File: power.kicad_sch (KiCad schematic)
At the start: 161 parts, among them Q10 SI7613DN-T1-GE3, Q14 BC817-25W, Q15 BC817-25W, Q2 BC817-25W, Q3 DZDH0401DW, Q4 DZDH0401DW, Q5 SI7613DN-T1-GE3, Q6 SI7613DN-T1-GE3, Q7 BC817-25W, Q8 BC817-25W, Q9 SI7613DN-T1-GE3, U1 LT8350RV#PBF, U10 LM3881MME_NOPB, U2 MP2386GG, U3 TPS65983BAZBHR, U9 LM1117MP-3.3_NOPB

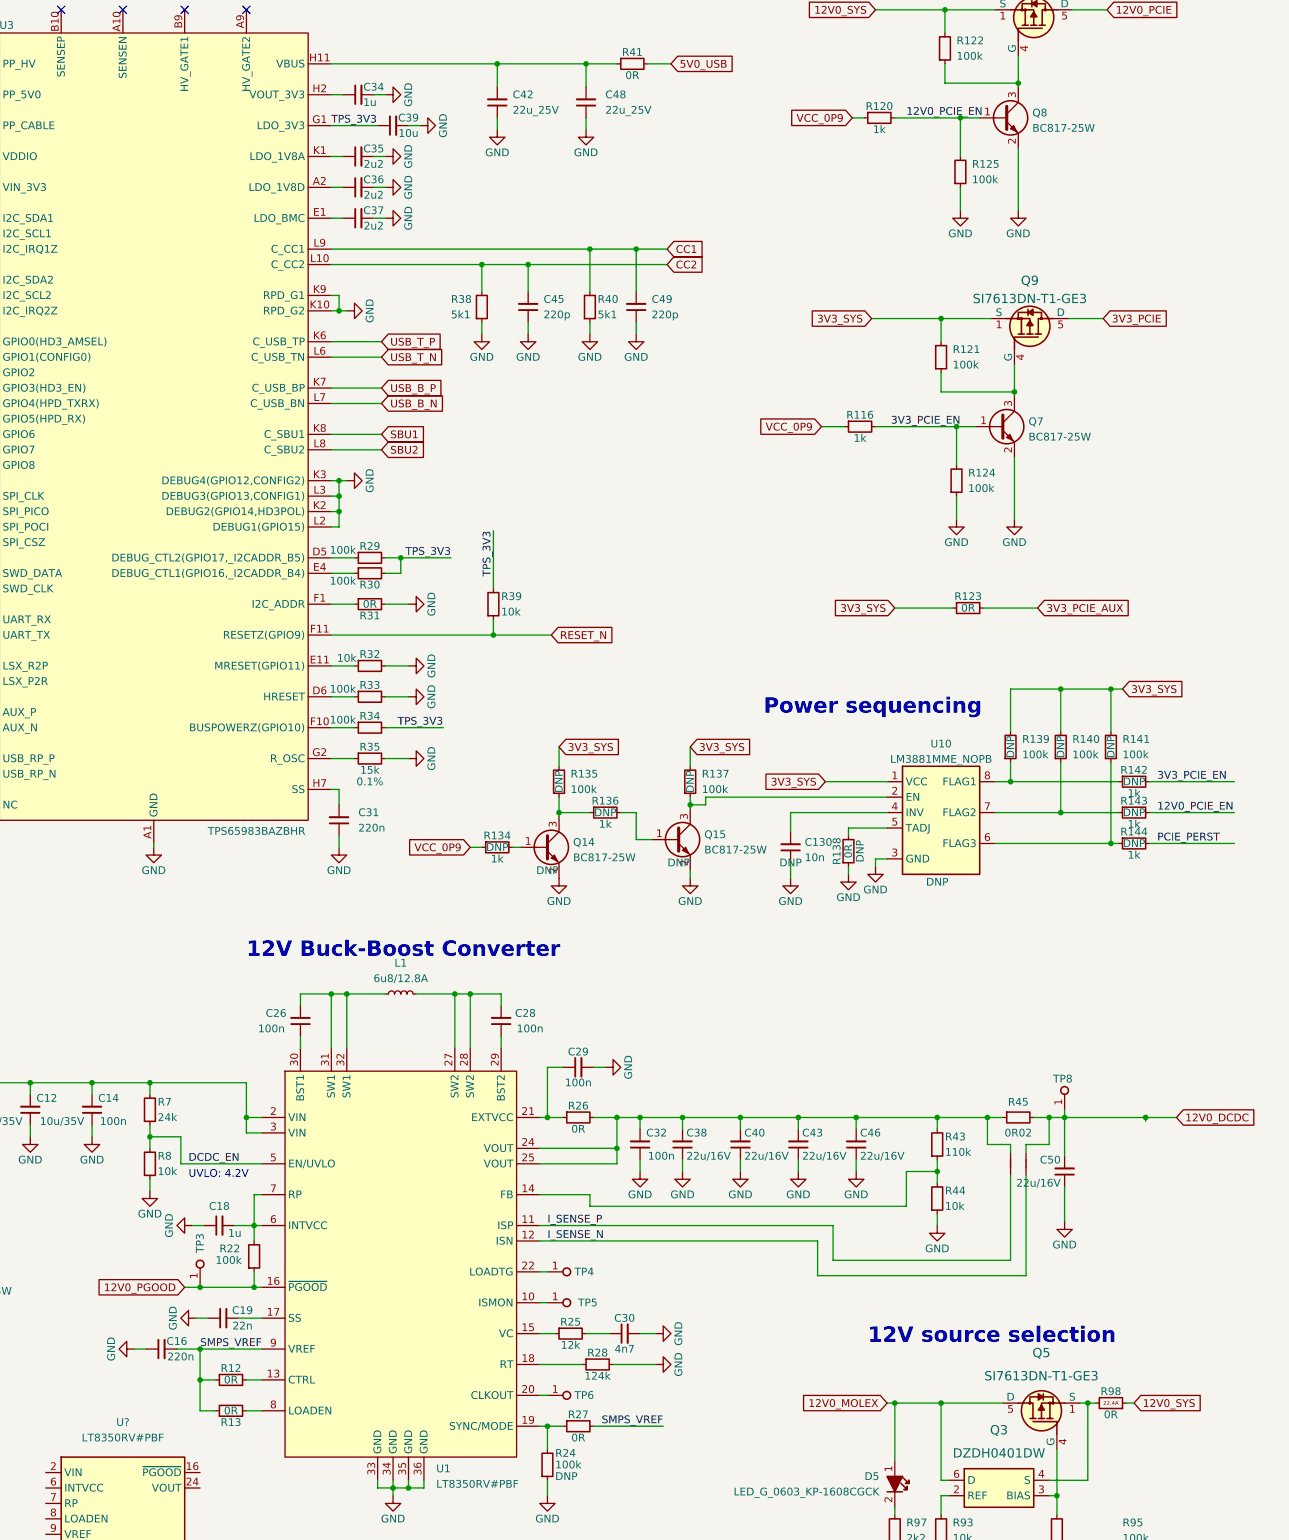
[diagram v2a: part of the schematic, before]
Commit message: Update PCIe power switching circuit (SCH)
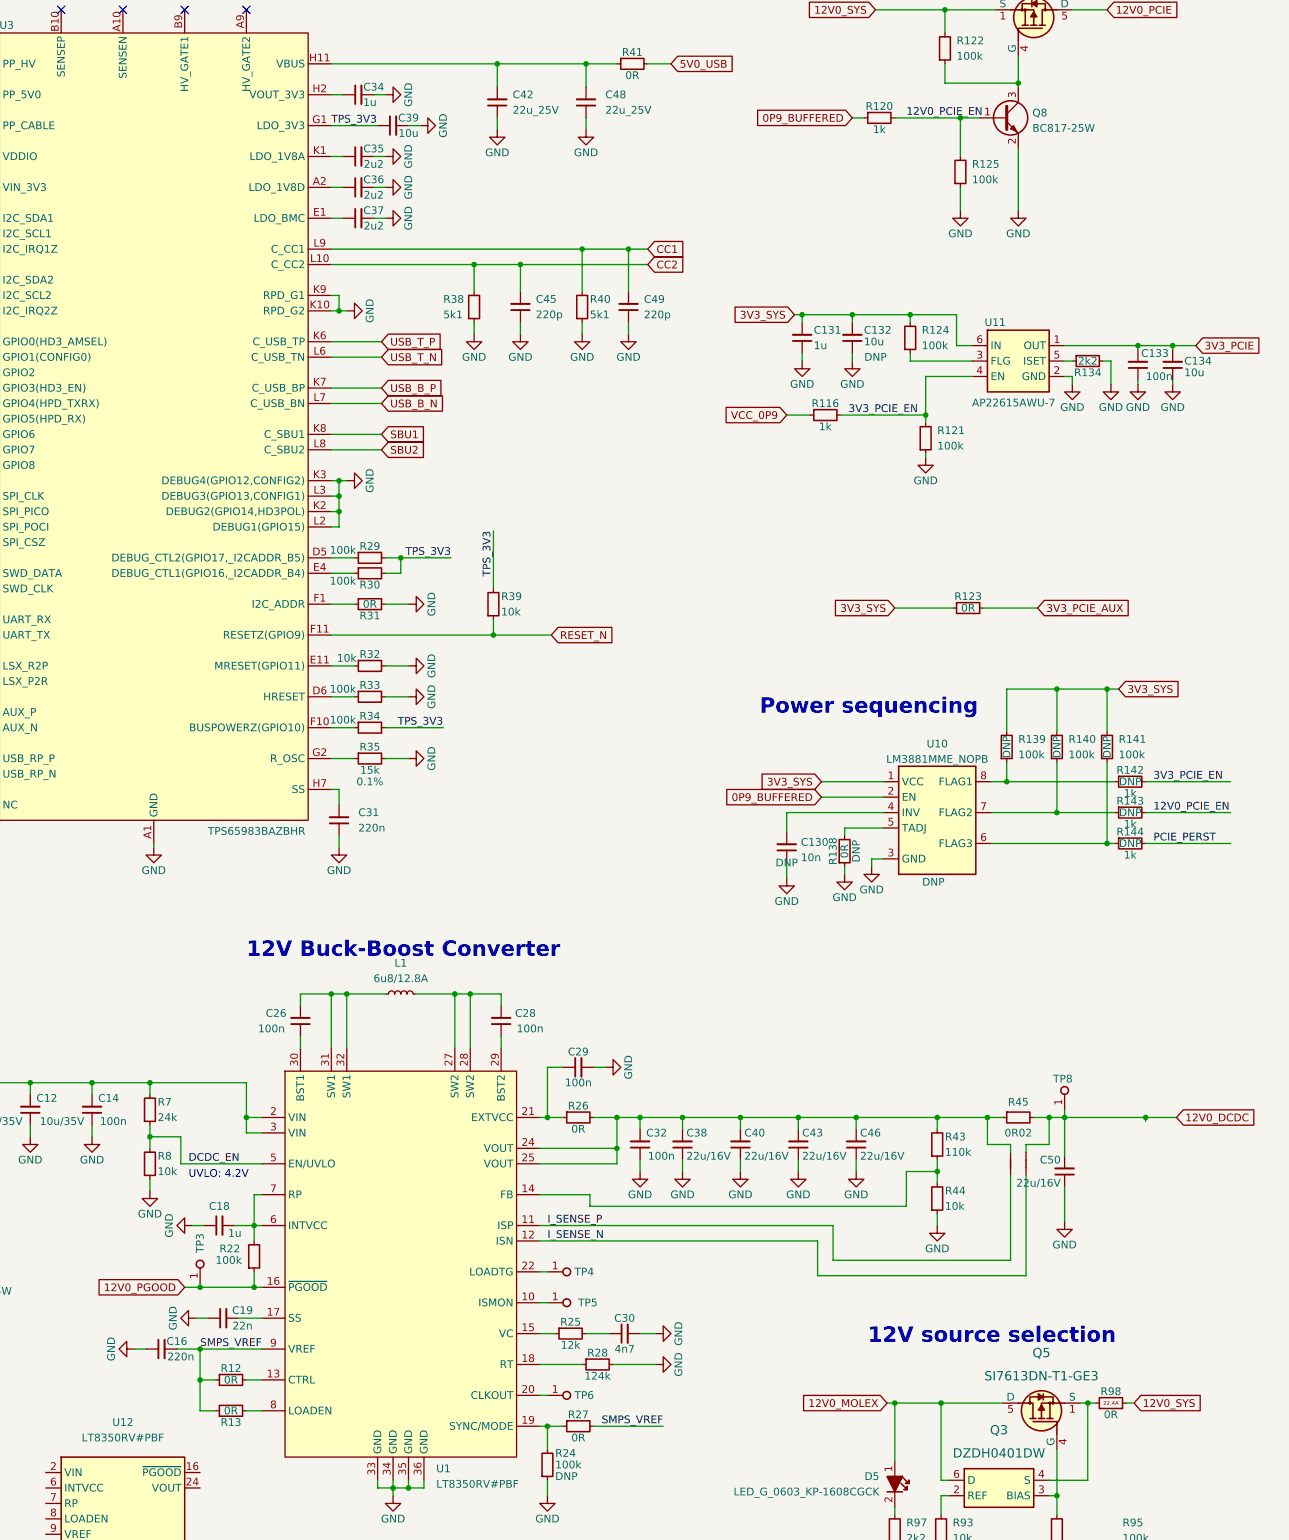
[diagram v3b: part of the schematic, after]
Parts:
- removed Q14, Q15, Q7: BC817-25W, thunderbolt-gpu-adapter-footprints:SOT-323, symbol thunderbolt-gpu-adapter:BC817-25W
- removed Q9: SI7613DN-T1-GE3, thunderbolt-gpu-adapter-footprints:Vishay_PowerPAK_1212-8_Single, symbol thunderbolt-gpu-adapter:SI7613DN-T1-GE3
- removed R134, R136: R_1k_0402, thunderbolt-gpu-adapter-footprints:R_0402_1005Metric, symbol thunderbolt-gpu-adapter:R_1k_0402
- removed R135, R137: R_100k_0402, thunderbolt-gpu-adapter-footprints:R_0402_1005Metric, symbol thunderbolt-gpu-adapter:R_100k_0402
- added C131: C_1u_0402, antmicro-footprints:C_0402_1005Metric, symbol antmicroCapacitors0402:C_1u_0402
- added C132, C134: C_10u_0603, antmicro-footprints:C_0603_1608Metric, symbol antmicroCapacitors0603:C_10u_0603
- added C133: C_100n_0402, thunderbolt-gpu-adapter-footprints:C_0402_1005Metric, symbol thunderbolt-gpu-adapter:C_100n_0402
- added R134: R_2k2_0402, antmicro-footprints:R_0402_1005Metric, symbol antmicroResistors0402:R_2k2_0402
- added U11: AP22615A_TSOT26, antmicro-footprints:TSOT23-6, symbol antmicroPMICPowerDistributionSwitchesLoadDrivers:AP22615A_TSOT26
- gave numbers to parts that had none: 1
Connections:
- net 3V3_PCIE: now also C133.2, C134.2, U11.1 (OUT)
- net 3V3_PCIE_EN: now also R121.2, U11.4 (EN); no longer R124.2
- net 3V3_SYS: now also R124.2, C131.2, C132.2, U11.6 (IN); no longer R121.2
- net GND: now also R121.1, C131.1, C132.1, C133.1, C134.1, R134.2, U11.2 (GND); no longer R124.1
- net VCC_0P9: no longer R120.1
- net 0P9_BUFFERED: now reaches U10.2 (EN)
- net 0P9_BUFFERED: now also R120.1
- new net: R124.1, U11.3 (FLG)
- new net: R134.1, U11.5 (ISET)
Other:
- moved on the sheet: C130, C45, C49, R116, R121, R138, R139, R140, R141, R142, R143, R144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

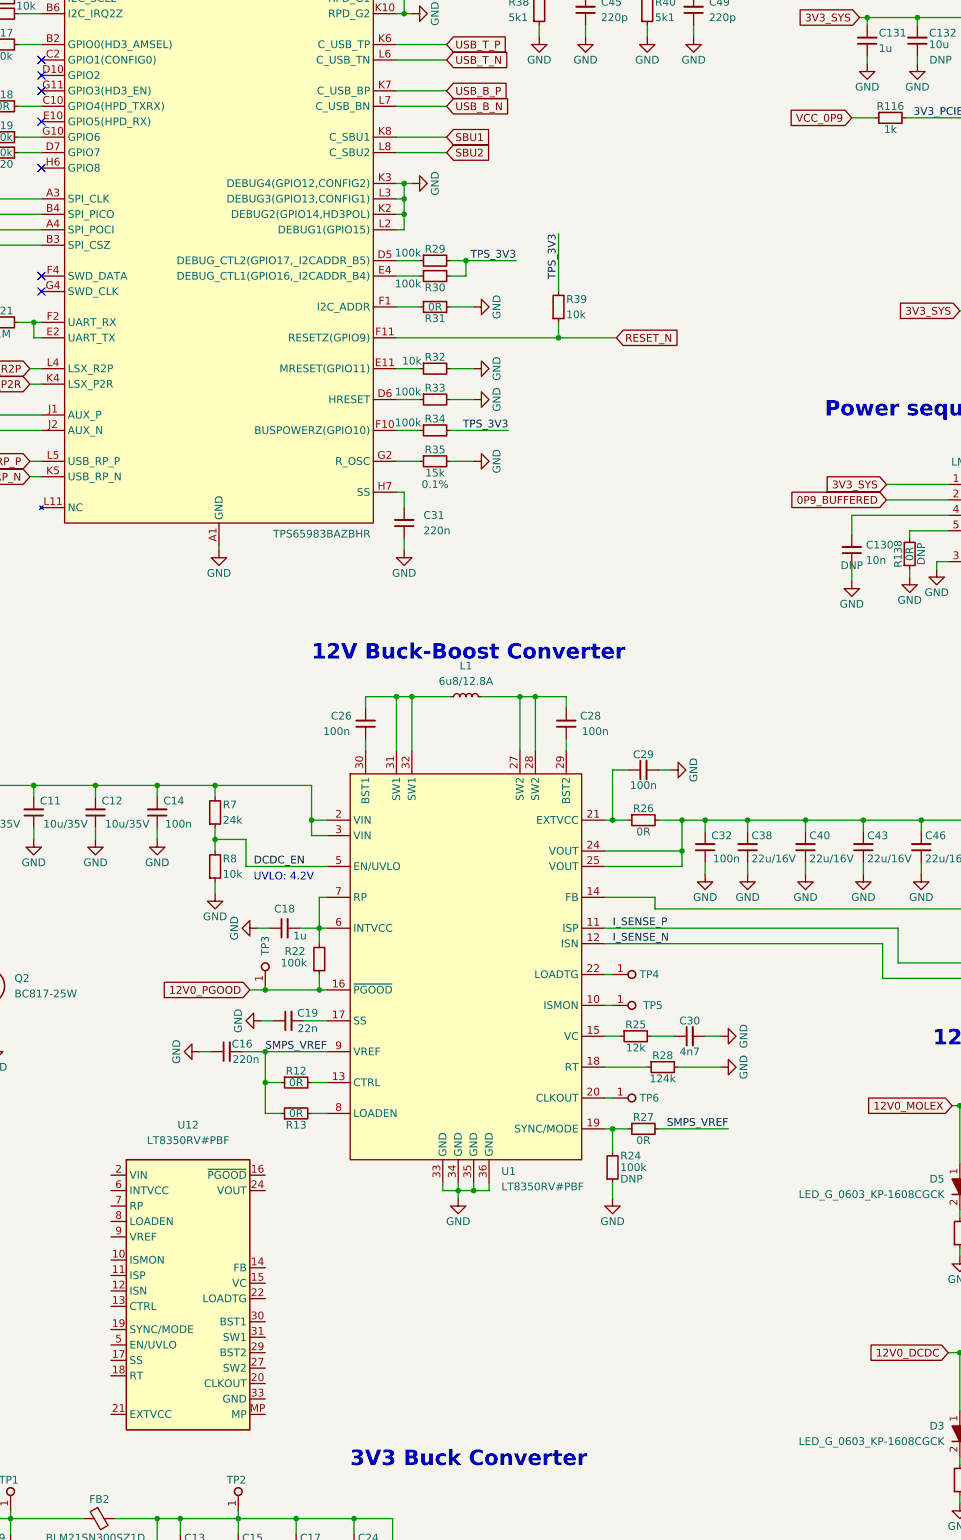
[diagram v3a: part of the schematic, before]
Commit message: Fix PCIe power switch - layout, bump revision to 1.1.2
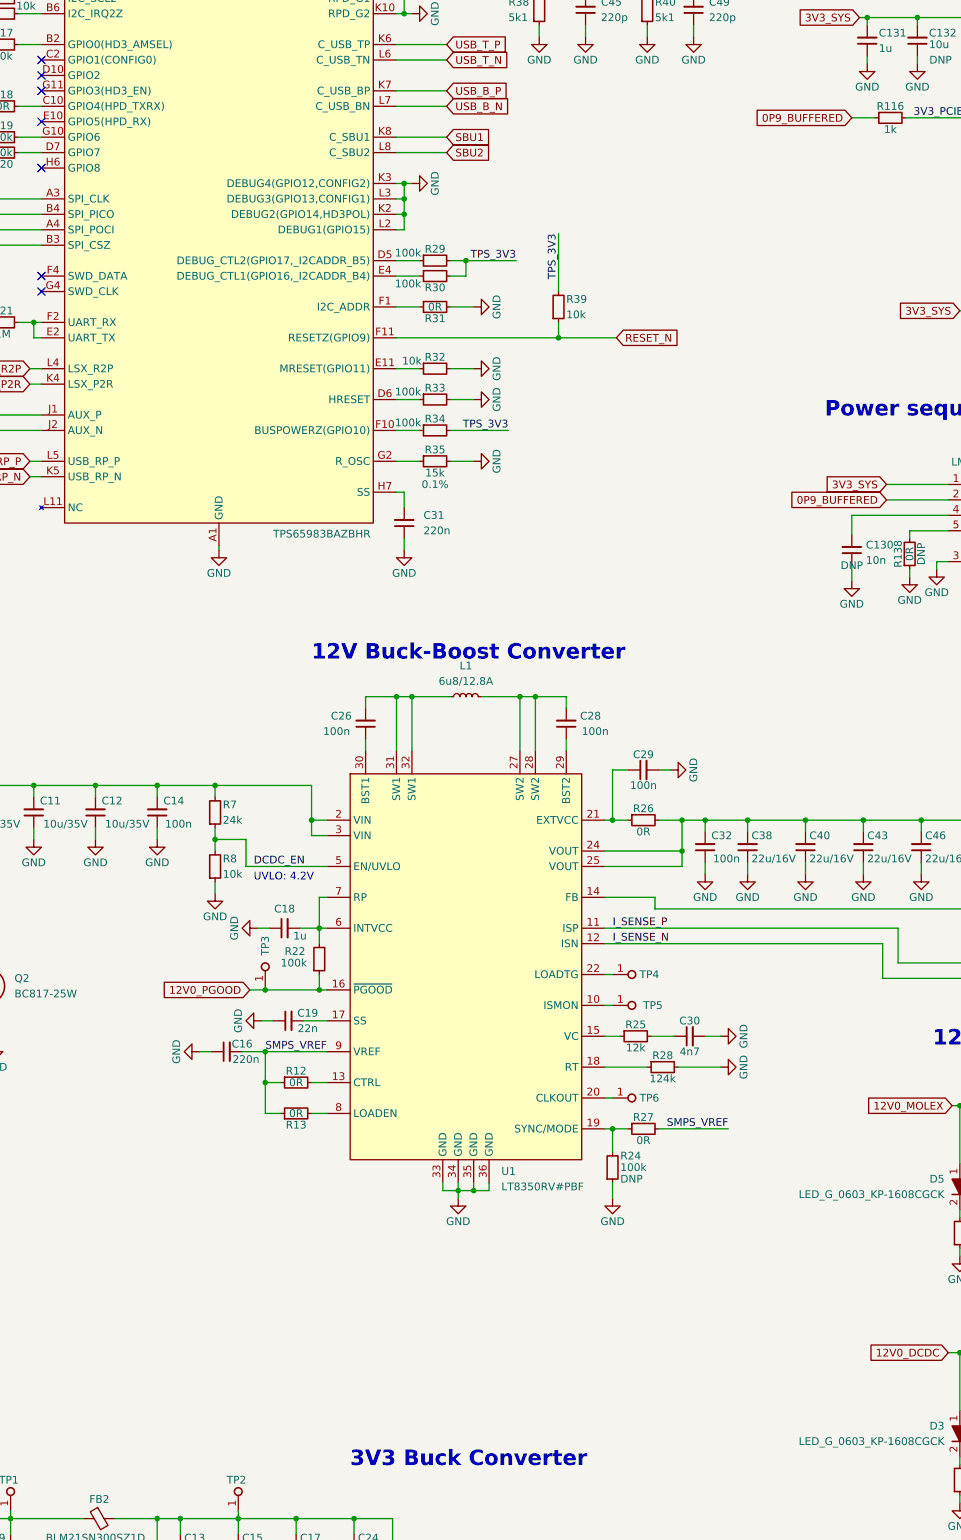
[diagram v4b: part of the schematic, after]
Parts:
- removed U12: LT8350RV, thunderbolt-gpu-adapter-footprints:QFN-32-4EP_4x6mm_P0.5mm, symbol thunderbolt-gpu-adapter:LT8350RV
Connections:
- net VCC_0P9 is gone; now on net 0P9_BUFFERED: R116.1
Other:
- company: (none) -> Antmicro Ltd
- title: (none) -> Thunderbolt GPU Adapter
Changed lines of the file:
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@@
   (paper "A3" portrait)
   (title_block
-    (date "2023-05-09")
-    (rev "1.1.1")
+    (title "Thunderbolt GPU Adapter")
+    (date "2023-11-21")
+    (rev "1.1.2")
+    (company "Antmicro Ltd")
     (comment 1 "www.antmicro.com")
-    (comment 2 "Antmicro Ltd.")
   )
   (junction (at 92.075 209.55) (diameter 0) (color 0 0 0 0)
@@
     )
   )
+  (global_label "0P9_BUFFERED" (shape input) (at 206.375 99.695 180) (fields_autoplaced)
+    (effects (font (size 1.27 1.27)) (justify right))
+    (property "Intersheet References" "${INTERSHEET_REFS}" (id 0) (at 189.6895 99.6156 0)
+      (effects (font (size 1.27 1.27)) (justify right) hide)
+    )
+  )
   (global_label "3V3_SYS" (shape input) (at 212.09 160.02 180) (fields_autoplaced)
     (effects (font (size 1.27 1.27)) (justify right))
@@
     )
   )
-  (global_label "VCC_0P9" (shape input) (at 206.375 99.695 180) (fields_autoplaced)
-    (effects (font (size 1.27 1.27)) (justify right))
-    (property "Intersheet References" "${INTERSHEET_REFS}" (id 0) (at 195.6767 99.7744 0)
-      (effects (font (size 1.27 1.27)) (justify right) hide)
-    )
-  )
   (global_label "CC1" (shape input) (at 183.515 72.39 0) (fields_autoplaced)
     (effects (font (size 1.27 1.27)) (justify left))
@@
     (pin "2")
   )
-  (symbol (lib_id "thunderbolt-gpu-adapter:LT8350RV") (at 84.455 273.685 0) (unit 1)
-    (in_bom yes) (on_board yes) (fields_autoplaced)
-    (property "Reference" "U12" (id 0) (at 97.155 265.43 0)
-      (effects (font (size 1.27 1.27) (thickness 0.15)))
-    )
-    (property "Value" "LT8350RV" (id 1) (at 141.605 283.845 0)
-      (effects (font (size 1.27 1.27) (thickness 0.15)) (justify left bottom) hide)
-    )
-    (property "Footprint" "thunderbolt-gpu-adapter-footprints:QFN-32-4EP_4x6mm_P0.5mm" (id 2) (at 141.605 286.385 0)
-      (effects (font (size 1.27 1.27) (thickness 0.15)) (justify left bottom) hide)
-    )
-    (property "Datasheet" "https://www.analog.com/media/en/technical-documentation/data-sheets/lt8350.pdf" (id 3) (at 141.605 288.925 0)
-      (effects (font (size 1.27 1.27) (thickness 0.15)) (justify left bottom) hide)
-    )
-    (property "MPN" "LT8350RV#PBF" (id 4) (at 97.155 267.97 0)
-      (effects (font (size 1.27 1.27) (thickness 0.15)))
-    )
-    (property "Manufacturer" "Analog Devices" (id 5) (at 141.605 291.465 0)
-      (effects (font (size 1.27 1.27) (thickness 0.15)) (justify left bottom) hide)
-    )
-    (property "License" "Apache-2.0" (id 6) (at 141.605 294.005 0)
-      (effects (font (size 1.27 1.27) (thickness 0.15)) (justify left bottom) hide)
-    )
-    (property "Author" "Antmicro" (id 7) (at 141.605 296.545 0)
-      (effects (font (size 1.27 1.27) (thickness 0.15)) (justify left bottom) hide)
-    )
-    (pin "10")
-    (pin "11")
-    (pin "12")
-    (pin "13")
-    (pin "14")
-    (pin "15")
-    (pin "16")
-    (pin "17")
-    (pin "18")
-    (pin "19")
-    (pin "2")
-    (pin "20")
-    (pin "21")
-    (pin "22")
-    (pin "24")
-    (pin "25")
-    (pin "27")
-    (pin "28")
-    (pin "29")
-    (pin "3")
-    (pin "30")
-    (pin "31")
-    (pin "32")
-    (pin "33")
-    (pin "34")
-    (pin "35")
-    (pin "36")
-    (pin "5")
-    (pin "6")
-    (pin "7")
-    (pin "8")
-    (pin "9")
-    (pin "MP")
-  )
   (symbol (lib_id "antmicroResistors0402:R_2k2_0402") (at 253.365 90.805 0) (unit 1)

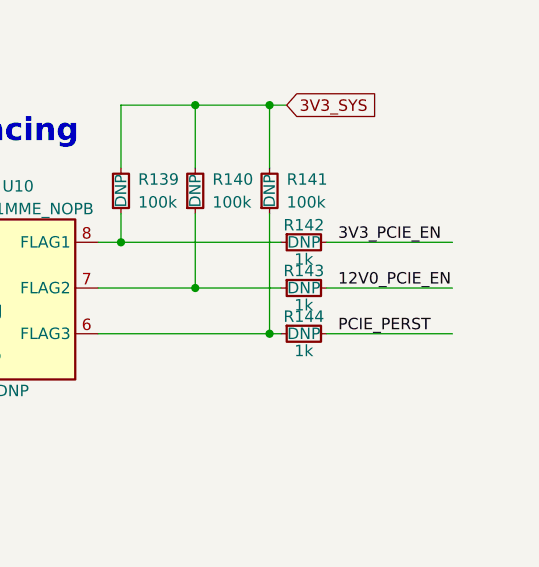
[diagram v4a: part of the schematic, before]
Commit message: [#51657][Schematic] Fix label names DRCs
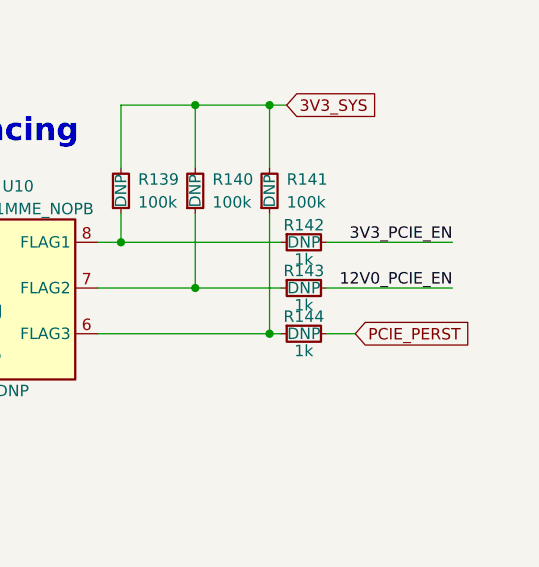
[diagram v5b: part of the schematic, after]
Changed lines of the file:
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@@
     (stroke (width 0) (type default) (color 0 0 0 0))
   )
-  (wire (pts (xy 265.43 170.18) (xy 279.4 170.18))
+  (wire (pts (xy 265.43 170.18) (xy 268.605 170.18))
     (stroke (width 0) (type default) (color 0 0 0 0))
   )
@@
     (effects (font (size 1.27 1.27)) (justify right bottom))
   )
-  (label "PCIE_PERST" (at 266.7 170.18 0)
-    (effects (font (size 1.27 1.27)) (justify left bottom))
-  )
   (label "I_SENSE_P" (at 167.005 233.045 0)
     (effects (font (size 1.27 1.27)) (justify left bottom))
@@
     (effects (font (size 1.27 1.27)) (justify right bottom))
   )
-  (label "3V3_PCIE_EN" (at 266.7 160.02 0)
-    (effects (font (size 1.27 1.27)) (justify left bottom))
+  (label "3V3_PCIE_EN" (at 279.4 160.02 180)
+    (effects (font (size 1.27 1.27)) (justify right bottom))
   )
   (label "3V3_PCIE_EN" (at 216.535 99.695 0)
@@
     (effects (font (size 1.27 1.27)) (justify left bottom))
   )
-  (label "12V0_PCIE_EN" (at 266.7 165.1 0)
-    (effects (font (size 1.27 1.27)) (justify left bottom))
+  (label "12V0_PCIE_EN" (at 279.4 165.1 180)
+    (effects (font (size 1.27 1.27)) (justify right bottom))
   )
   (label "SMPS_LDO" (at 167.64 359.41 180)
@@
     )
   )
+  (global_label "PCIE_PERST" (shape input) (at 268.605 170.18 0) (fields_autoplaced)
+    (effects (font (size 1.27 1.27)) (justify left))
+    (property "Intersheet References" "${INTERSHEET_REFS}" (id 0) (at 282.1457 170.1006 0)
+      (effects (font (size 1.27 1.27)) (justify left) hide)
+    )
+  )
